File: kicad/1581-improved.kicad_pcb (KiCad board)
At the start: 2 copper layers, 184 x 112 mm, 84 parts, among them CN1 IEC, CN2 FLOPPY, CN3 DIN6, CN4 DIN6, CN5 CN5, J1 DRVPWR, J2 12VDC, J3 12V-IN, J4 GND, SW1 DS02-254-1L-02BE, SW2 300DP1J1BLKM7QE, U1 MOS6502AD, U10 74LS93, U11 74LS07, U12 SN7406N, U13 74LS241, U14 74LVC1G08GV, U15 V7805-2000R, U2 27C512, U3 62256, U4 WD1770, U5 MOS6520, U6 74LS139, U7 74LS00, U8 SN7406N, U9 74LS14, X1 ACO-16.000MHZ-EK

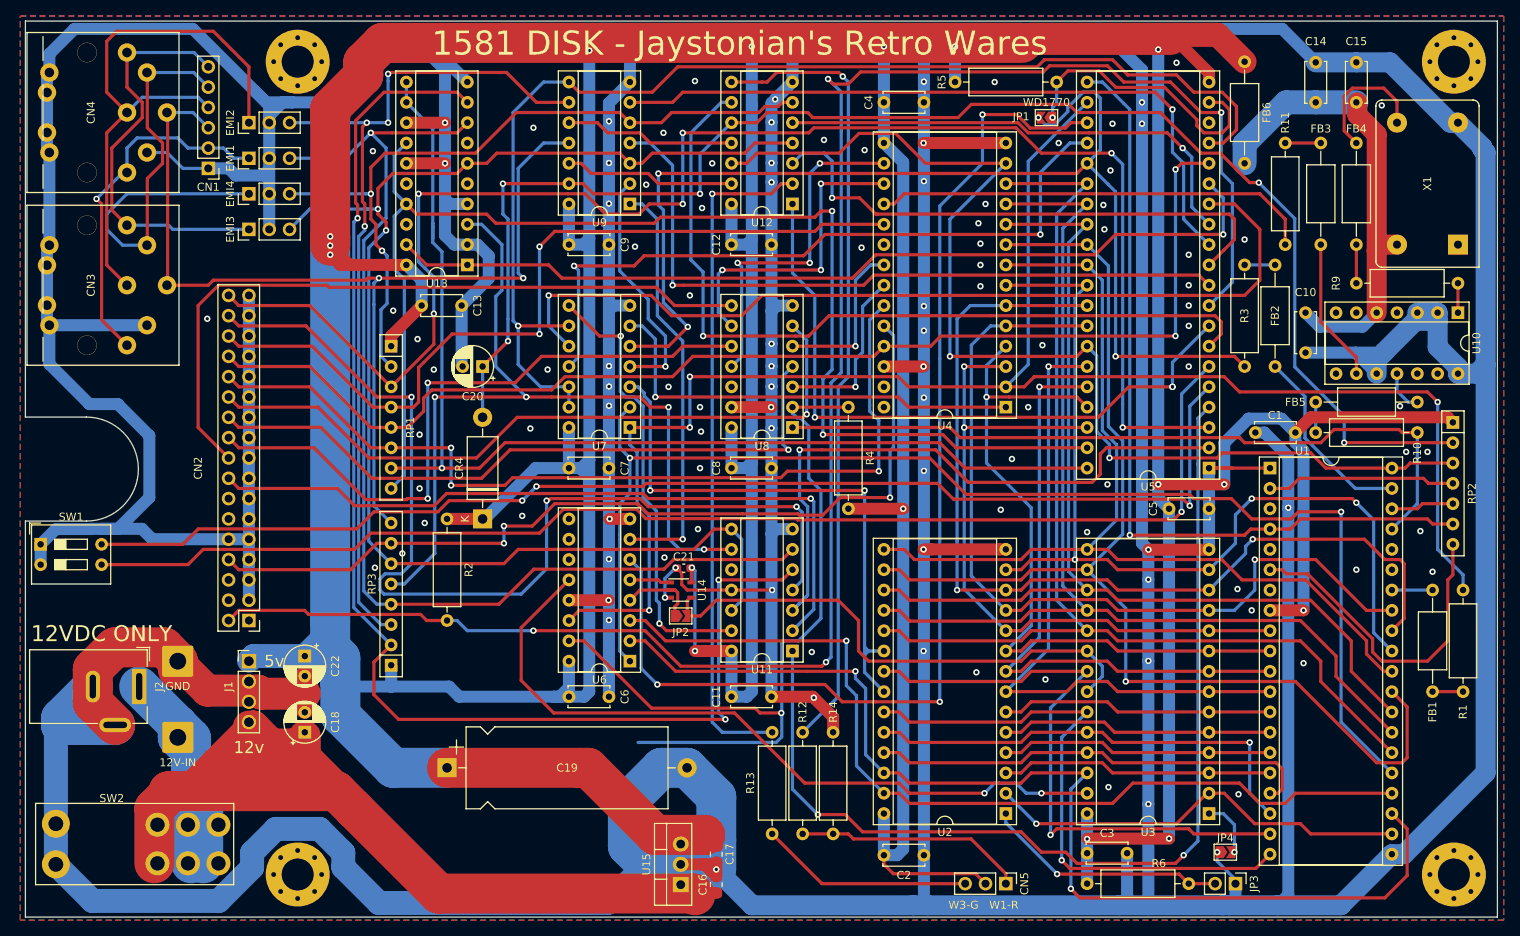
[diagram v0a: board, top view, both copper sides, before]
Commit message: Typo on 6520 -> 8520/6526
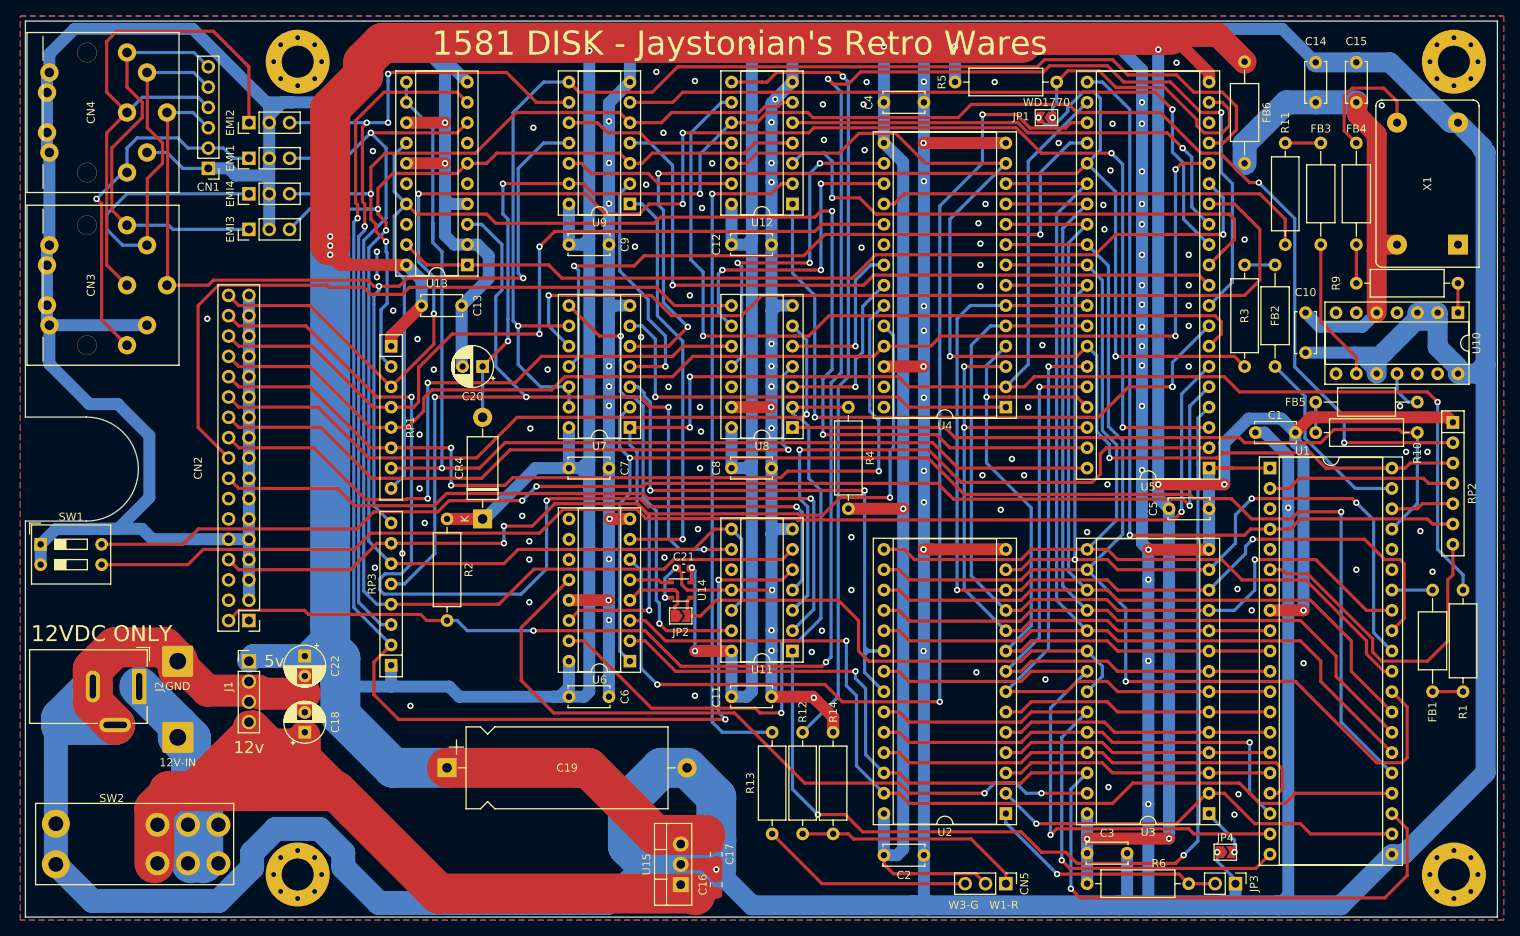
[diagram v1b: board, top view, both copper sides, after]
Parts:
- U5: value MOS6520 -> MOS8520/6526
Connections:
- net /E~ATN renamed /E~{ATN}
- net /R~W renamed /R~{W}
- net /~ATN renamed /~{ATN}
- net /~DIRC renamed /~{DIRC}
- net /~DISKCH renamed /~{DISKCH}
- net /~FLAG renamed /~{FLAG}
- net /~IP renamed /~{IP}
- net /~IRQ renamed /~{IRQ}
- net /~MOTOR renamed /~{MOTOR}
- net /~MOTORX renamed /~{MOTORX}
- net /~NMI renamed /~{NMI}
- net /~RAMOE renamed /~{RAMOE}
- net /~RAMWE renamed /~{RAMWE}
- net /~RD renamed /~{RD}
- net /~RDY renamed /~{RDY}
- net /~RESET renamed /~{RESET}
- net /~RESET0 renamed /~{RESET0}
- net /~RESET2 renamed /~{RESET2}
- net /~ROMOE renamed /~{ROMOE}
- net /~RWE renamed /~{RWE}
- net /~SO renamed /~{SO}
- net /~STEP renamed /~{STEP}
- net /~TR00 renamed /~{TR00}
- net /~VIASEL renamed /~{VIASEL}
- net /~WD renamed /~{WD}
- net /~WDSEL renamed /~{WDSEL}
- net /~WDSEL2 renamed /~{WDSEL2}
- net /~WG renamed /~{WG}
- net /~WPRT renamed /~{WPRT}
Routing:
- net /~{RWE}: track 101.5 -> 80.3 mm
- net GND: track 1466.1 -> 1469.2 mm, vias 113 -> 145
- net Net-(JP4-Pad2): track 7.18 -> 6.14 mm
- net /~{DIRC}: track 89.4 -> 90.1 mm
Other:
- net class Default removed
